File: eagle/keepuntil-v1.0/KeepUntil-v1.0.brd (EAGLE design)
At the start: 100 x 80 mm, 17 parts, among them IC2 REG1117, J1 USB-MICROB, Q1 CSTCR6M00G53Z, T1 BC846, U1 ATMEGA328P-AU

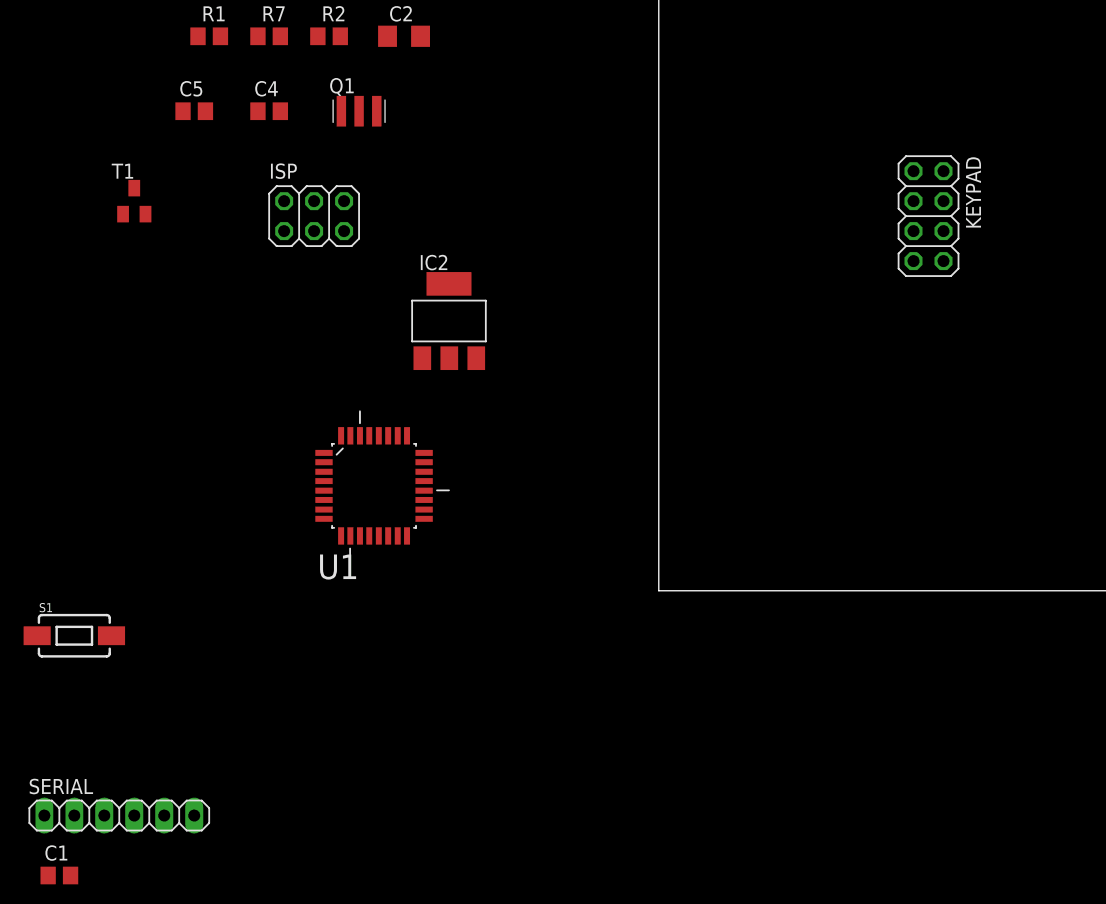
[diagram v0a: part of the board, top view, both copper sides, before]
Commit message: schematic cleanup and board
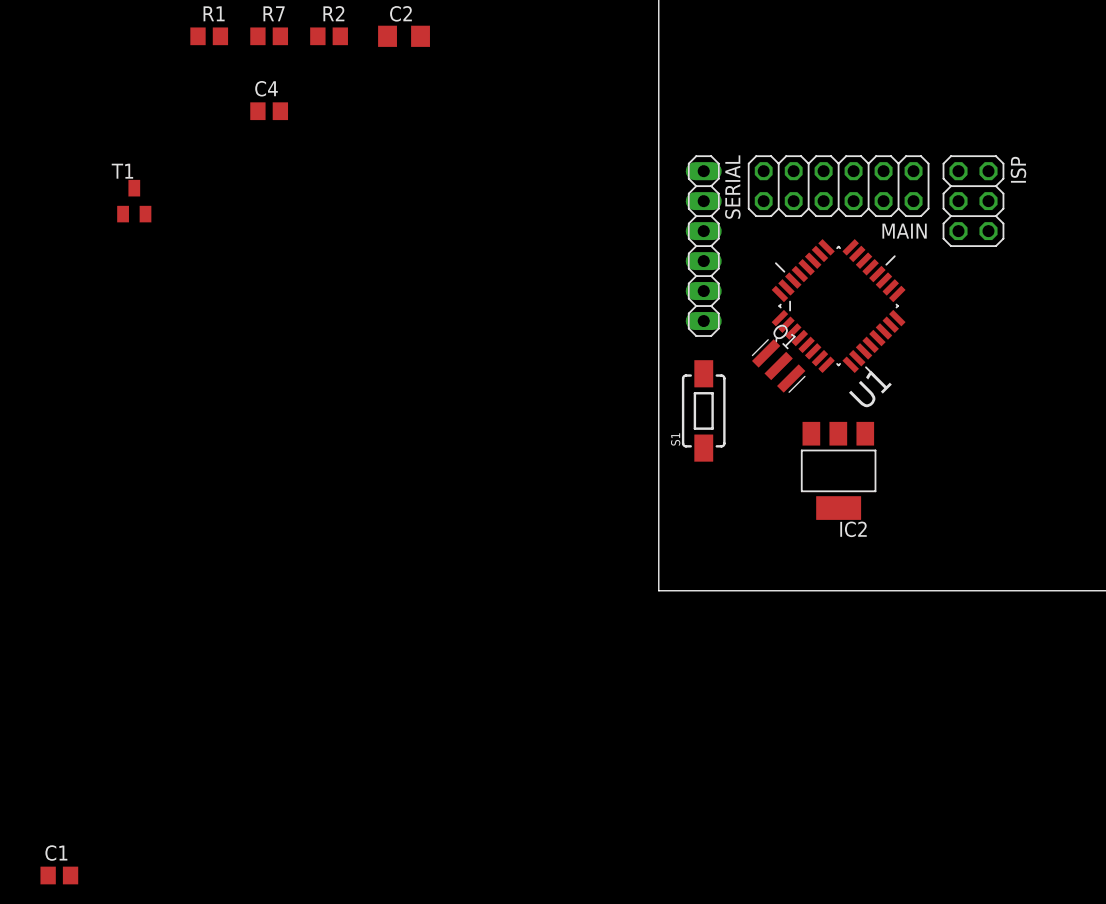
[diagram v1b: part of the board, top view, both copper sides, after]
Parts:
- removed C5: 0.1uF, resistor:C0805
- removed KEYPAD: (no value), pinhead:2X04
- added MAIN: (no value), pinhead:2X06
- moved SERIAL 69.2 mm to (3.81, 29.2), turned to 270 degrees
- moved S1 56.6 mm to (3.81, 15.2), turned to 90 degrees
- moved ISP 55.9 mm to (26.7, 33.0), turned to 270 degrees
- moved U1 42.2 mm to (15.2, 24.1), turned to 45 degrees
- moved Q1 41.6 mm to (10.2, 19.1), turned to 315 degrees
- moved IC2 35.4 mm to (15.2, 10.2), turned to 180 degrees
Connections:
- removed net COL1: KEYPAD.1
- removed net COL2: KEYPAD.3
- removed net COL3: KEYPAD.5
- removed net N$10: U1.11
- removed net N$11: U1.12
- removed net N$12: U1.13
- removed net N$13: U1.14
- removed net N$14: U1.24
- removed net N$15: U1.25
- removed net N$16: U1.26
- removed net N$5: U1.23
- removed net N$6: U1.9
- removed net N$8: C5.1, U1.20
- removed net N$9: U1.10
- removed net ROW1: KEYPAD.2
- removed net ROW2: KEYPAD.4
- removed net ROW3: KEYPAD.6
- removed net ROW4: KEYPAD.8
- removed net SCL: U1.28
- removed net SDA: U1.27
- new net BT-RX: MAIN.2, U1.23
- new net BT-TX: MAIN.4, U1.24
- new net RTC-SCL: MAIN.12, U1.28
- new net RTC-SDA: MAIN.10, U1.27
- new net SERVO: MAIN.8, U1.26
- net GND: now also MAIN.11, MAIN.3, MAIN.7; no longer C5.2
- net MISO: now also ISP.3; no longer ISP.5
- net MOSI: now also ISP.5; no longer ISP.1
- net SCK: now also ISP.1; no longer ISP.3
- net SOLENOID-SIG: now also MAIN.6, U1.25
- net VCC: now also MAIN.1, MAIN.5, MAIN.9
